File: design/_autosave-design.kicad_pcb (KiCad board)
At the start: 2 copper layers, 73.7 x 68.6 mm, 29 parts, among them J1 Conn_01x03_Pin, J2 Conn_01x02_Pin, J3 Conn_01x02_Pin, U1 MC7912, U2 L7812, U3 OPA209AID, U4 TL082

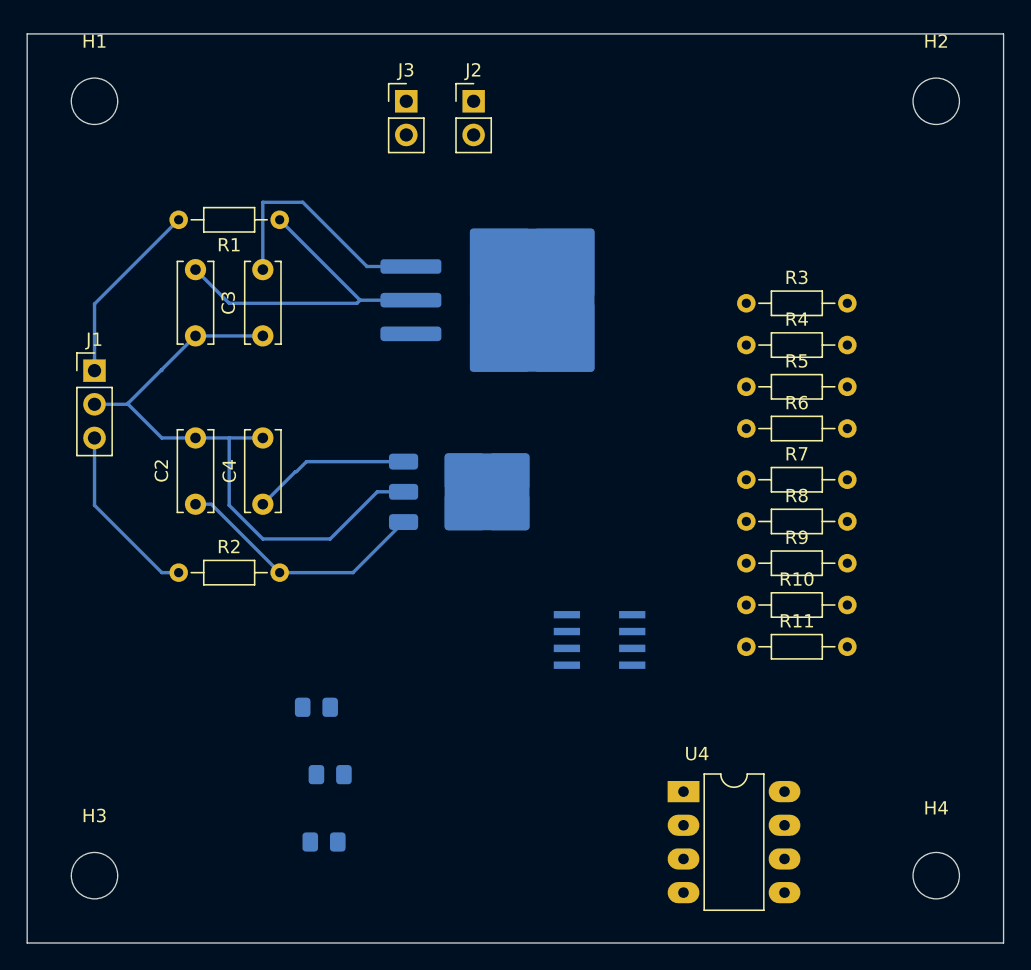
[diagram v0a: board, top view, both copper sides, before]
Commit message: Cambios muy importantes en PCB y schematic de KiCad
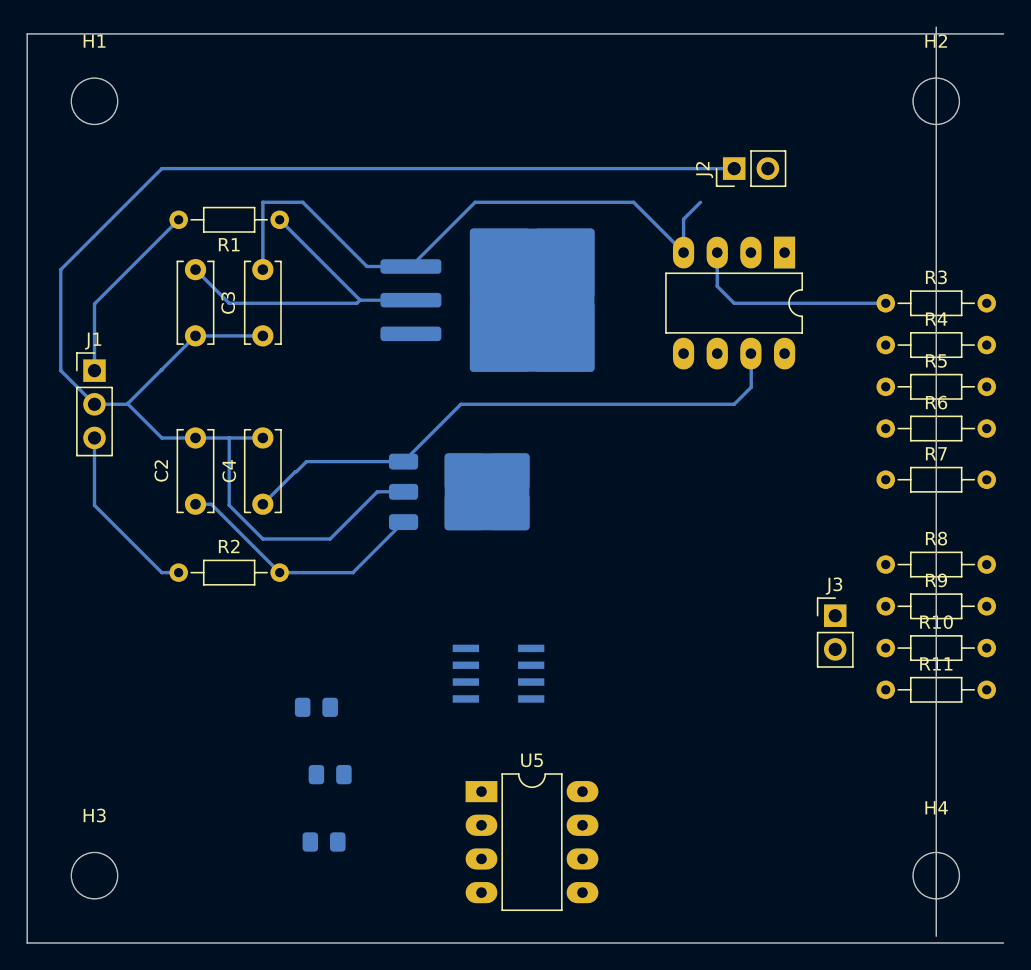
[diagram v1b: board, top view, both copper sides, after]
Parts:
- added U5: TL081, Package_DIP:DIP-8_W7.62mm_LongPads, F.Cu at (138.4, 113.0)
- U4: value TL082 -> TL081
- moved J3 50.5 mm to (165.1, 99.8)
- moved U4 41.4 mm to (161.3, 72.4), turned to -90 degrees
- moved J2 20.3 mm to (157.5, 66.0), turned to 90 degrees
- moved R10 11.0 mm to (168.9, 102.2)
- moved R11 11.0 mm to (168.9, 105.4)
- moved R8 11.0 mm to (168.9, 95.9)
- moved R9 11.0 mm to (168.9, 99.1)
- moved R3 10.5 mm to (168.9, 76.2)
- moved R4 10.5 mm to (168.9, 79.3)
- moved R5 10.5 mm to (168.9, 82.5)
- moved R6 10.5 mm to (168.9, 85.7)
- moved R7 10.5 mm to (168.9, 89.5)
- moved U3 8.03 mm to (139.7, 104.1)
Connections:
- R10 pad 1: Net-(U4B--) -> Net-(U5-+)
- R11 pad 2: Net-(U4B--) -> Net-(U5-+)
- U4 pad 1: Net-(R3-Pad2) -> unconnected-(U4-NULL-Pad1)
- U4 pad 4: (no net) -> -12V
- U4 pad 5: Earth -> unconnected-(U4-NULL-Pad5)
- U4 pad 6: Net-(U4B--) -> Net-(R3-Pad2)
- U4 pad 7: Net-(J3-Pin_1) -> +12V
- U4 pad 8: (no net) -> unconnected-(U4-NC-Pad8)
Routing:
- net Earth: track 46.9 -> 112.1 mm
- net +12V: track 11.9 -> 43.0 mm
- net -12V: track 18.3 -> 46.8 mm
- net load: track 0.00 -> 15.8 mm
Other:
- board size 73.7 x 68.6 mm -> 73.7 x 69.1 mm
